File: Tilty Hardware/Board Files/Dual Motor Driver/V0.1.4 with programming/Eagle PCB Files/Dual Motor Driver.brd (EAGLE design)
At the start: 38.4 x 50.8 mm, 43 parts, among them J1 AVR_SPI_PRG_62X3_LOCK, Q1 16MHz, U1 ATMEGA328P, U2 L298_BRIDGE_DRIVER, U3 LM2931

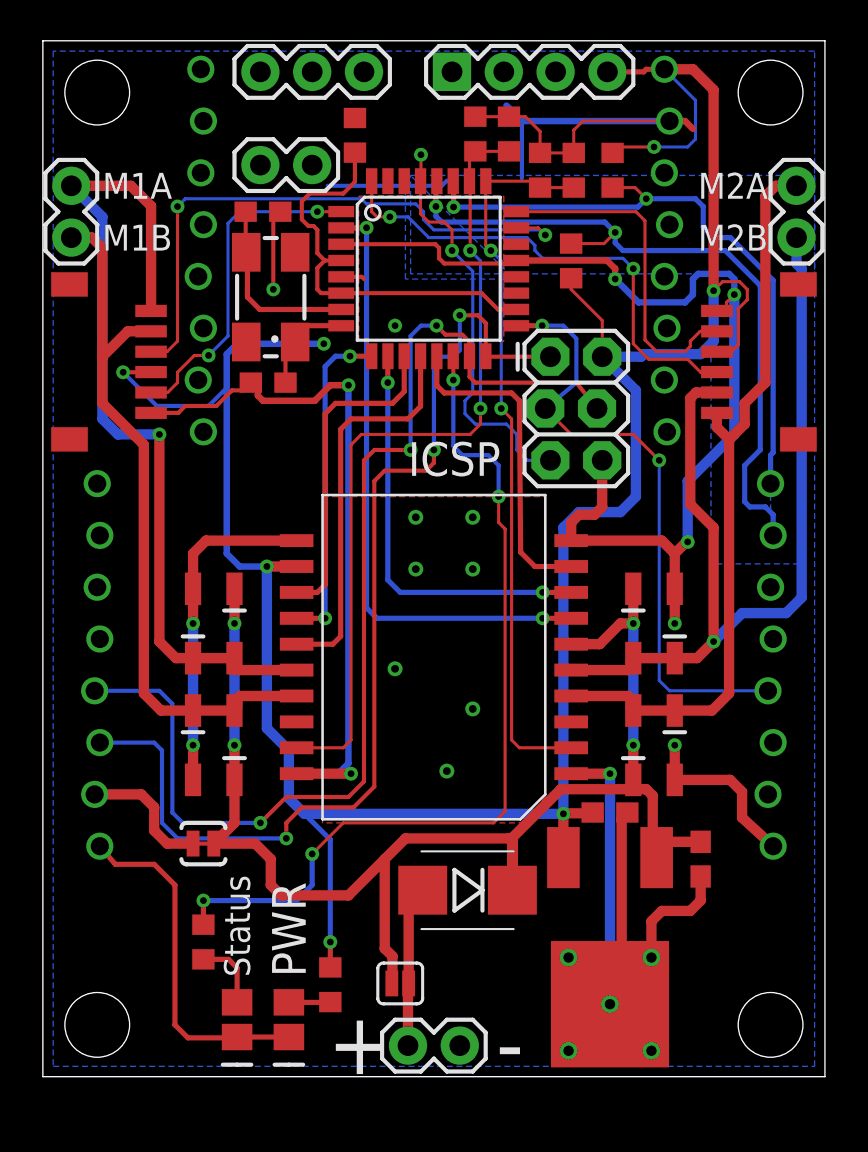
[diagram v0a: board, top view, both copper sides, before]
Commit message: Nicely laid out Dual Motor Driver with programming capability
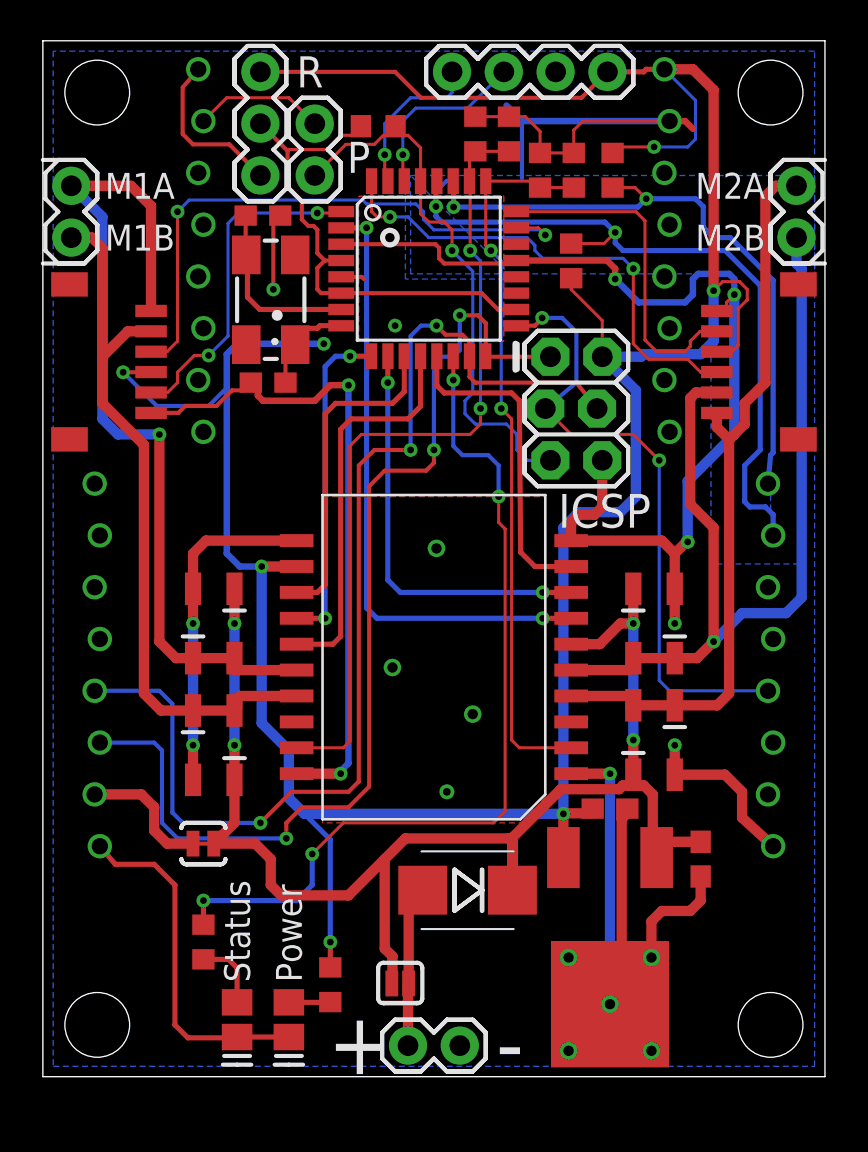
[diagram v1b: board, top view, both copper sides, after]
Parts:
- moved JP12 5.08 mm to (10.7, 44.2), turned to 90 degrees
- moved JP7 3.35 mm to (13.3, 46.7), turned to 270 degrees
- moved R1 1.23 mm to (16.4, 46.6), turned to 180 degrees
- moved D1 0.25 mm to (31.0, 16.5)
- moved D8 0.25 mm to (29.0, 16.5)
- moved C6 0.19 mm to (27.8, 13.1)
- moved C8 0.19 mm to (10.8, 42.2)
- moved Q1 0.13 mm to (11.2, 38.1)
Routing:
- net +5V: track 134.7 -> 153.0 mm
- net RX: track 0.01 -> 8.94 mm, vias 0 -> 1
- net +3V3: track 0.00 -> 8.11 mm
- net TX: track 0.00 -> 7.83 mm, vias 0 -> 1
- net RESET: track 20.0 -> 26.9 mm, vias 2 -> 1
- net RST: track 0.00 -> 6.46 mm
- net GND: track 209.5 -> 203.6 mm, vias 24 -> 21
- net POWER: track 20.5 -> 24.8 mm
- net SCK: track 30.3 -> 30.9 mm
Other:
- board text added: "P"
- board text added: "Power"
- board text added: "R"
- board text added: "RST"
- board text removed: "PWR"
